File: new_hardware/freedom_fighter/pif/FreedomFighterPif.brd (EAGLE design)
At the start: 160 x 100 mm, 15 parts, among them U1 PIA6821, U4 HD68A09EP, U5 74LS74D, U9 DM74LS04N

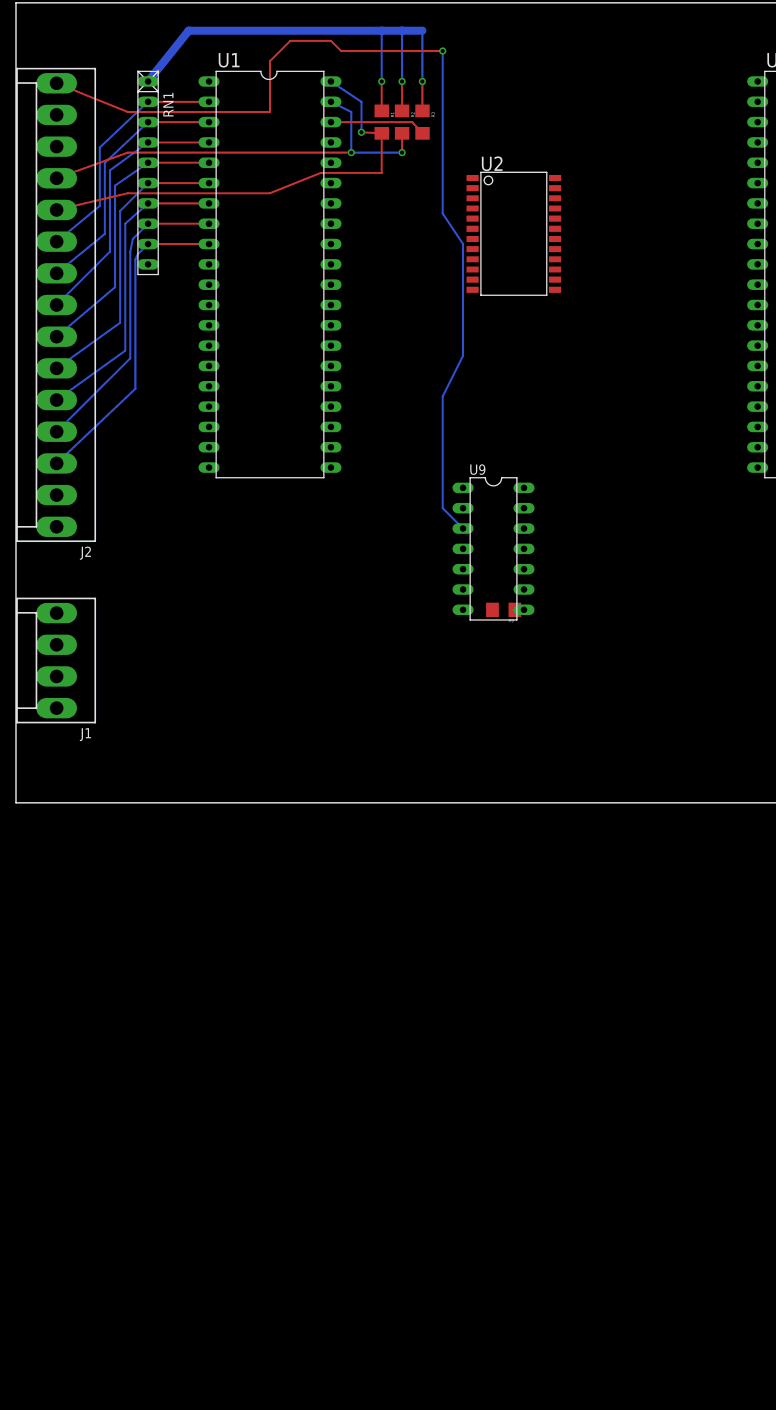
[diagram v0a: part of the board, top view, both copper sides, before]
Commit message: did more reverse engineering of freedom fighter pif board
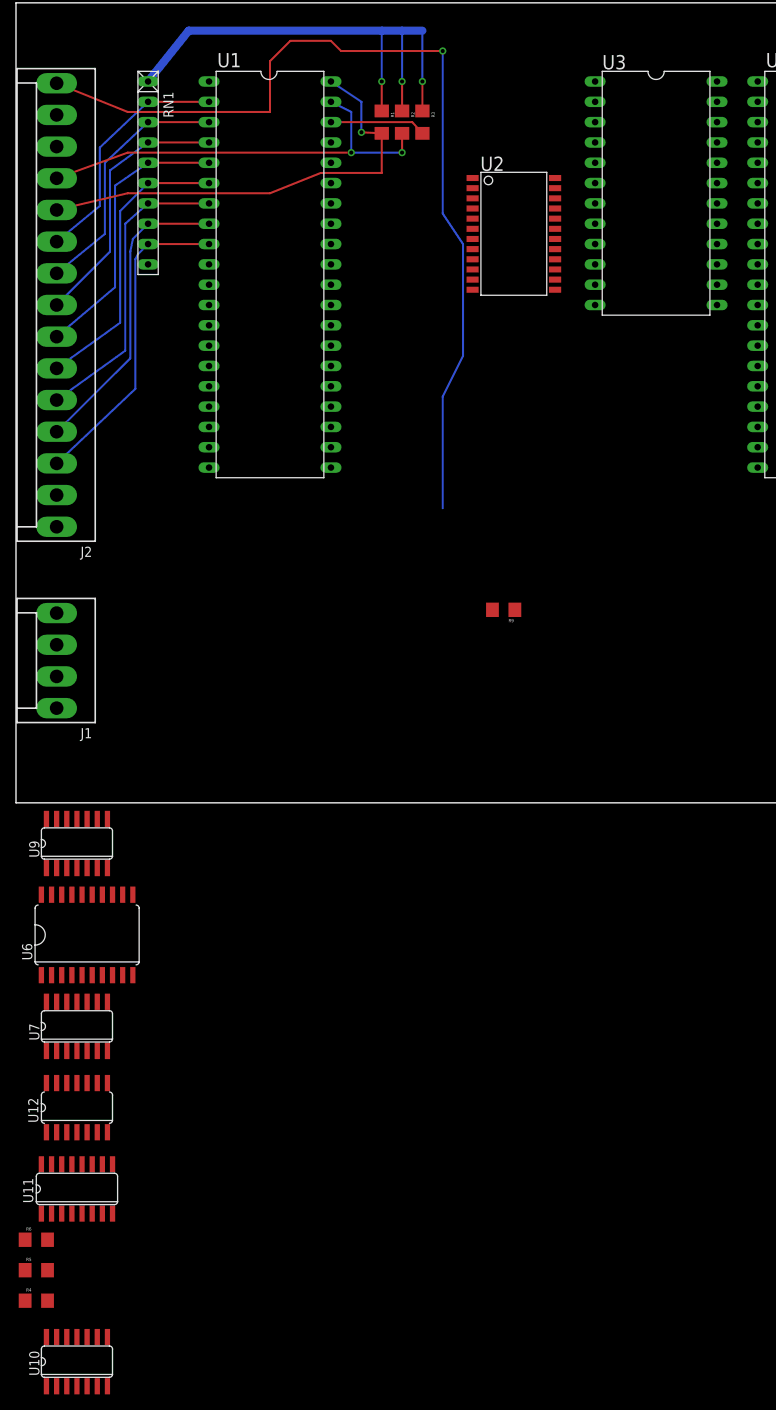
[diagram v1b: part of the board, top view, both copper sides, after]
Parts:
- added R4, R5, R6: 4.7k, SparkFun:1206
- added U10: 74LS74D, 74xx-us:SO14
- added U11: 74LS138D, 74xx-us:SO16
- added U12: 74LS125D, 74xx-eu:SO14
- added U3: 2732, memory:DIL24
- added U6: 74LS245DW, 74xx-us:SO20W
- added U7: 74LS10D, 74xx-us:SO14
- U9: value DM74LS04N -> 74LS04D; device ic-package:DIL14 -> 74xx-us:SO14
- moved U9 63.8 mm to (7.62, -5.08), turned to 0 degrees
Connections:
- removed net !IRQA: R3.2, U1.38
- new net !E: U10.2, U10.8
- new net !HALT: R4.2, U4.40
- new net !IRQA/FIRQ: R3.2, U1.38, U4.4
- new net !IRQB/NMI: R5.2, U4.2
- new net !Q: U10.6, U7.4, U7.5
- new net 4MHZ: U10.11, U10.3
- new net A13: U11.1, U4.21
- new net A14: U11.2, U4.22
- new net A15: U11.3, U4.23
- new net E: U10.9
- new net N$4: U11.6, U7.6
- new net N$6: U7.3
- new net Q: U10.12, U10.5
- new net R/!W: U1.21, U2.21, U4.32, U6.1, U7.1, U9.1
- net !IRQ: now also R6.2
- net GND: now also U10.7, U11.4, U11.5, U11.8, U12.7, U3.12, U4.1, U6.10, U7.7, U9.7
- net VCC: now also R4.1, R5.1, R6.1, U10.14, U11.16, U12.14, U3.24, U6.20, U7.14, U9.14
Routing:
- net !IRQA/FIRQ: track 0.00 -> 12.1 mm
- net !IRQA: track 12.1 -> 0.00 mm
- net EVEN/!ODD: track 119.0 -> 115.4 mm

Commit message: more reverse engineering
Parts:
- removed U3: 2732, memory:DIL24
- added C100: Unknown value, SparkFun:1206
- added DB1: DB25, mpo:A32077-ND
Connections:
- removed net N$6: U7.3
- new net !ENABLE_DAVDAK: U11.14, U12.1, U12.13
- new net !ENABLE_PIA: U1.23, U11.11
- new net !ENABLE_RAM: U11.15, U2.18
- new net !ENABLE_ROM: U11.7, U12.4
- new net !ENABLE_ROM_CE: U12.6
- new net !ENABLE_U12C: U11.9, U12.10
- new net !ENABLE_VP931_DATA: U11.12, U6.19, U9.9
- new net !VP931_RDEN: DB1.P10, U7.12
- new net !VP931_WREN: DB1.P22, U7.8
- new net D1: U4.30, U6.17
- new net D2: U4.29, U6.16
- new net D3: U4.28, U6.15
- new net D4: U4.27, U6.14
- new net D5: U4.26, U6.13
- new net D6: U12.11, U4.25, U6.12
- new net D7: U12.3, U4.24, U6.11
- new net ENABLE_VP931_DATA: U7.10, U7.13, U9.8
- new net VP931_D0: DB1.P14, U6.2
- new net VP931_D1: DB1.P15, U6.3
- new net VP931_D2: DB1.P16, U6.4
- new net VP931_D3: DB1.P17, U6.5
- new net VP931_D4: DB1.P18, U6.6
- new net VP931_D5: DB1.P19, U6.7
- new net VP931_D6: DB1.P20, U6.8
- new net VP931_D7: DB1.P21, U6.9
- new net VP931_DAK: DB1.P23, U12.2
- new net VP931_DAV: DB1.P11, U12.12
- new net W/!R: U2.20, U7.9, U9.2
- net !E: now also U7.3
- net D0: now also U6.18
- net E: now also C100.2, U4.34, U7.2
- net GND: now also DB1.P9, U12.5, U12.9, U5.10; no longer U3.12
- net Q: now also U4.35, U7.11
- net VCC: now also C100.1; no longer U3.24

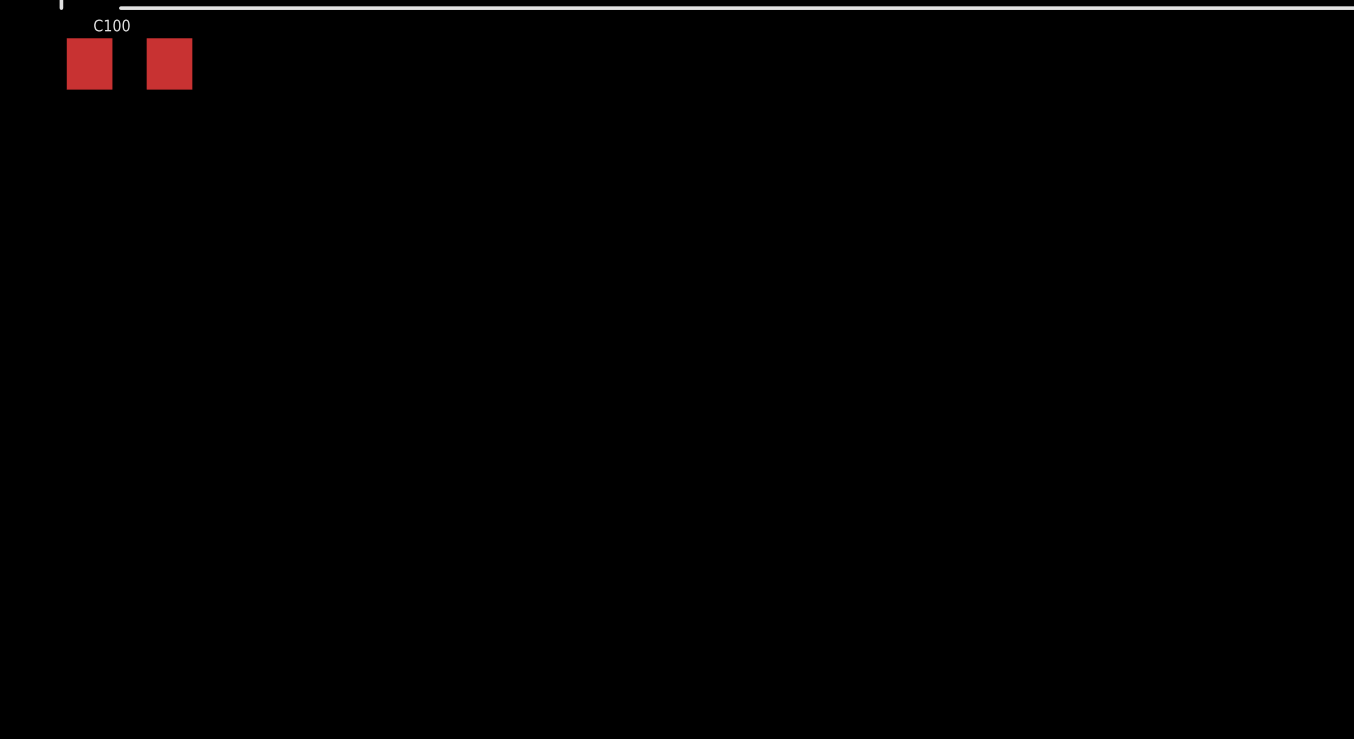
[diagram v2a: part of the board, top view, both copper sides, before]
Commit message: added FFR PIF disassembly and updated PIF schematics
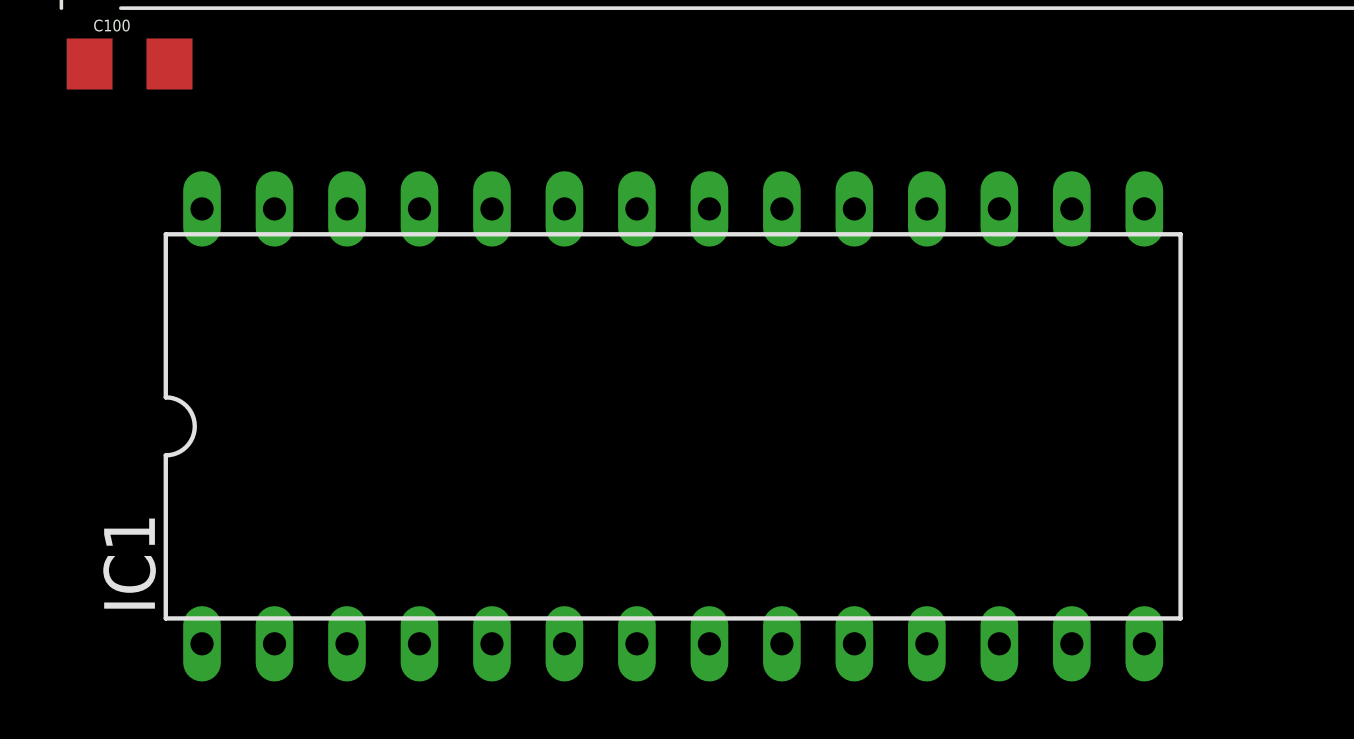
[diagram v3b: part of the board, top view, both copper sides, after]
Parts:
- added IC1: (no value), memory:DIL28
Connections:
- new net A0: IC1.10, U4.8
- new net A1: IC1.9, U4.9
- new net A10: IC1.21, U4.18
- new net A11: IC1.23, U4.19
- new net A12: IC1.2, U4.20
- new net A2: IC1.8, U4.10
- new net A3: IC1.7, U4.11
- new net A4: IC1.6, U4.12
- new net A5: IC1.5, U4.13
- new net A6: IC1.4, U4.14
- new net A7: IC1.3, U4.15
- new net A8: IC1.25, U4.16
- new net A9: IC1.24, U4.17
- net !ENABLE_ROM_CE: now also IC1.20
- net A13: now also IC1.26
- net D0: now also IC1.19
- net D1: now also IC1.18
- net D2: now also IC1.11
- net D3: now also IC1.16
- net D4: now also IC1.15
- net D5: now also IC1.13
- net D6: now also IC1.12
- net D7: now also IC1.17
- net GND: now also IC1.14, IC1.22, U4.39
- net VCC: now also IC1.1, IC1.27, IC1.28, U4.7
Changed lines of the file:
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@@
 <element name="DB1" library="mpo" package="A32077-ND" value="DB25" x="26.67" y="-90.17"/>
 <element name="C100" library="SparkFun" package="1206" value="Unknown value" x="2.54" y="-95.25"/>
+<element name="IC1" library="memory" package="DIL28" value="" x="21.59" y="-107.95"/>
 </elements>
 <signals>
@@
 <contactref element="U12" pad="9"/>
 <contactref element="U5" pad="10"/>
+<contactref element="IC1" pad="14"/>
+<contactref element="U4" pad="39"/>
+<contactref element="IC1" pad="22"/>
 <wire x1="128.8034" y1="82.55" x2="139.7" y2="90.3" width="0" layer="19" extent="1-1"/>
 <wire x1="122.6566" y1="80.01" x2="128.8034" y2="82.55" width="0" layer="19" extent="1-1"/>
-<wire x1="92.71" y1="90.17" x2="122.6566" y2="80.01" width="0" layer="19" extent="1-1"/>
+<wire x1="107.95" y1="87.63" x2="122.6566" y2="80.01" width="0" layer="19" extent="1-1"/>
+<wire x1="92.71" y1="90.17" x2="107.95" y2="87.63" width="0" layer="19" extent="1-1"/>
 <wire x1="57.0738" y1="64.135" x2="92.71" y2="90.17" width="0" layer="19" extent="1-1"/>
 <wire x1="24.13" y1="90.17" x2="57.0738" y2="64.135" width="0" layer="19" extent="1-1"/>
@@
 <wire x1="11.43" y1="-72.9234" x2="12.065" y2="-51.3334" width="0" layer="19" extent="1-1"/>
 <wire x1="32.1903" y1="-91.5924" x2="11.43" y2="-72.9234" width="0" layer="19" extent="1-1"/>
+<wire x1="20.32" y1="-100.33" x2="32.1903" y2="-91.5924" width="0" layer="19" extent="1-1"/>
+<wire x1="38.1" y1="-115.57" x2="20.32" y2="-100.33" width="0" layer="19" extent="1-1"/>
 </signal>
 <signal name="5V">
@@
 <contactref element="U10" pad="14"/>
 <contactref element="C100" pad="1"/>
+<contactref element="IC1" pad="28"/>
+<contactref element="U4" pad="7"/>
+<contactref element="IC1" pad="1"/>
+<contactref element="IC1" pad="27"/>
 <wire x1="132.08" y1="91.57" x2="135.89" y2="91.57" width="0" layer="19" extent="1-1"/>
 <wire x1="128.8034" y1="87.63" x2="132.08" y2="91.57" width="0" layer="19" extent="1-1"/>
-<wire x1="67.3862" y1="78.105" x2="128.8034" y2="87.63" width="0" layer="19" extent="1-1"/>
+<wire x1="92.71" y1="74.93" x2="128.8034" y2="87.63" width="0" layer="19" extent="1-1"/>
+<wire x1="67.3862" y1="78.105" x2="92.71" y2="74.93" width="0" layer="19" extent="1-1"/>
 <wire x1="50.8" y1="86.49" x2="67.3862" y2="78.105" width="0" layer="19" extent="1-1"/>
 <wire x1="62.36" y1="24.13" x2="67.3862" y2="78.105" width="0" layer="19" extent="1-1"/>
@@
 <wire x1="3.81" y1="-66.7766" x2="1.14" y2="-62.23" width="0" layer="19" extent="1-1"/>
 <wire x1="1.14" y1="-95.25" x2="3.81" y2="-66.7766" width="0" layer="19" extent="1-1"/>
+<wire x1="5.08" y1="-100.33" x2="1.14" y2="-95.25" width="0" layer="19" extent="1-1"/>
+<wire x1="7.62" y1="-100.33" x2="5.08" y2="-100.33" width="0" layer="19" extent="1-1"/>
+<wire x1="5.08" y1="-115.57" x2="5.08" y2="-100.33" width="0" layer="19" extent="1-1"/>
 </signal>
 <signal name="PA2">
@@
 <contactref element="U5" pad="2"/>
 <contactref element="U6" pad="18"/>
+<contactref element="IC1" pad="19"/>
 <wire x1="107.95" y1="67.31" x2="122.6566" y2="86.36" width="0" layer="19" extent="1-1"/>
 <wire x1="5.715" y1="-11.4808" x2="107.95" y2="67.31" width="0" layer="19" extent="1-1"/>
+<wire x1="27.94" y1="-100.33" x2="5.715" y2="-11.4808" width="0" layer="19" extent="1-1"/>
 </signal>
 <signal name="!IRQ">
@@
 <contactref element="U4" pad="21"/>
 <contactref element="U11" pad="1"/>
+<contactref element="IC1" pad="26"/>
 <wire x1="3.175" y1="-51.3334" x2="107.95" y2="41.91" width="0" layer="19" extent="1-1"/>
+<wire x1="10.16" y1="-100.33" x2="3.175" y2="-51.3334" width="0" layer="19" extent="1-1"/>
 </signal>
 <signal name="A14">
@@
 <contactref element="U6" pad="11"/>
 <contactref element="U12" pad="3"/>
+<contactref element="IC1" pad="17"/>
 <wire x1="14.605" y1="-11.4808" x2="107.95" y2="49.53" width="0" layer="19" extent="1-1"/>
 <wire x1="6.35" y1="-41.1734" x2="14.605" y2="-11.4808" width="0" layer="19" extent="1-1"/>
+<wire x1="33.02" y1="-100.33" x2="6.35" y2="-41.1734" width="0" layer="19" extent="1-1"/>
 </signal>
 <signal name="D6">
@@
 <contactref element="U12" pad="11"/>
 <contactref element="U6" pad="12"/>
+<contactref element="IC1" pad="12"/>
 <wire x1="13.335" y1="-11.4808" x2="107.95" y2="52.07" width="0" layer="19" extent="1-1"/>
 <wire x1="7.62" y1="-35.0266" x2="13.335" y2="-11.4808" width="0" layer="19" extent="1-1"/>
+<wire x1="33.02" y1="-115.57" x2="7.62" y2="-35.0266" width="0" layer="19" extent="1-1"/>
 </signal>
 <signal name="D5">
 <contactref element="U4" pad="26"/>
 <contactref element="U6" pad="13"/>
+<contactref element="IC1" pad="13"/>
 <wire x1="12.065" y1="-11.4808" x2="107.95" y2="54.61" width="0" layer="19" extent="1-1"/>
+<wire x1="35.56" y1="-115.57" x2="12.065" y2="-11.4808" width="0" layer="19" extent="1-1"/>
 </signal>
 <signal name="D4">
 <contactref element="U4" pad="27"/>
 <contactref element="U6" pad="14"/>
+<contactref element="IC1" pad="15"/>
 <wire x1="10.795" y1="-11.4808" x2="107.95" y2="57.15" width="0" layer="19" extent="1-1"/>
+<wire x1="38.1" y1="-100.33" x2="10.795" y2="-11.4808" width="0" layer="19" extent="1-1"/>
 </signal>
 <signal name="D3">
 <contactref element="U4" pad="28"/>
 <contactref element="U6" pad="15"/>
+<contactref element="IC1" pad="16"/>
 <wire x1="9.525" y1="-11.4808" x2="107.95" y2="59.69" width="0" layer="19" extent="1-1"/>
+<wire x1="35.56" y1="-100.33" x2="9.525" y2="-11.4808" width="0" layer="19" extent="1-1"/>
 </signal>
 <signal name="D2">
 <contactref element="U4" pad="29"/>
 <contactref element="U6" pad="16"/>
+<contactref element="IC1" pad="11"/>
 <wire x1="8.255" y1="-11.4808" x2="107.95" y2="62.23" width="0" layer="19" extent="1-1"/>
+<wire x1="30.48" y1="-115.57" x2="8.255" y2="-11.4808" width="0" layer="19" extent="1-1"/>
 </signal>
 <signal name="D1">
 <contactref element="U4" pad="30"/>
 <contactref element="U6" pad="17"/>
+<contactref element="IC1" pad="18"/>
 <wire x1="6.985" y1="-11.4808" x2="107.95" y2="64.77" width="0" layer="19" extent="1-1"/>
+<wire x1="30.48" y1="-100.33" x2="6.985" y2="-11.4808" width="0" layer="19" extent="1-1"/>
 </signal>
 <signal name="!ENABLE_VP931_DATA">
@@
 <signal name="!ENABLE_ROM_CE">
 <contactref element="U12" pad="6"/>
+<contactref element="IC1" pad="20"/>
+<wire x1="10.16" y1="-41.1734" x2="25.4" y2="-100.33" width="0" layer="19" extent="1-1"/>
 </signal>
 <signal name="!ENABLE_RAM">
@@
 <wire x1="4.445" y1="-45.1866" x2="67.3862" y2="70.485" width="0" layer="19" extent="1-1"/>
 </signal>
+<signal name="A0">
+<contactref element="U4" pad="8"/>
+<contactref element="IC1" pad="10"/>
+<wire x1="27.94" y1="-115.57" x2="92.71" y2="72.39" width="0" layer="19" extent="1-1"/>
+</signal>
+<signal name="A1">
+<contactref element="U4" pad="9"/>
+<contactref element="IC1" pad="9"/>
+<wire x1="25.4" y1="-115.57" x2="92.71" y2="69.85" width="0" layer="19" extent="1-1"/>
+</signal>
+<signal name="A2">
+<contactref element="U4" pad="10"/>
+<contactref element="IC1" pad="8"/>
+<wire x1="22.86" y1="-115.57" x2="92.71" y2="67.31" width="0" layer="19" extent="1-1"/>
+</signal>
+<signal name="A3">
+<contactref element="U4" pad="11"/>
+<contactref element="IC1" pad="7"/>
+<wire x1="20.32" y1="-115.57" x2="92.71" y2="64.77" width="0" layer="19" extent="1-1"/>
+</signal>
+<signal name="A4">
+<contactref element="U4" pad="12"/>
+<contactref element="IC1" pad="6"/>
+<wire x1="17.78" y1="-115.57" x2="92.71" y2="62.23" width="0" layer="19" extent="1-1"/>
+</signal>
+<signal name="A5">
+<contactref element="U4" pad="13"/>
+<contactref element="IC1" pad="5"/>
+<wire x1="15.24" y1="-115.57" x2="92.71" y2="59.69" width="0" layer="19" extent="1-1"/>
+</signal>
+<signal name="A6">
+<contactref element="U4" pad="14"/>
+<contactref element="IC1" pad="4"/>
+<wire x1="12.7" y1="-115.57" x2="92.71" y2="57.15" width="0" layer="19" extent="1-1"/>
+</signal>
+<signal name="A7">
+<contactref element="U4" pad="15"/>
+<contactref element="IC1" pad="3"/>
+<wire x1="10.16" y1="-115.57" x2="92.71" y2="54.61" width="0" layer="19" extent="1-1"/>
+</signal>
+<signal name="A8">
+<contactref element="U4" pad="16"/>
+<contactref element="IC1" pad="25"/>
+<wire x1="12.7" y1="-100.33" x2="92.71" y2="52.07" width="0" layer="19" extent="1-1"/>
+</signal>
+<signal name="A9">
+<contactref element="U4" pad="17"/>
+<contactref element="IC1" pad="24"/>
+<wire x1="15.24" y1="-100.33" x2="92.71" y2="49.53" width="0" layer="19" extent="1-1"/>
+</signal>
+<signal name="A10">
+<contactref element="U4" pad="18"/>
+<contactref element="IC1" pad="21"/>
+<wire x1="22.86" y1="-100.33" x2="92.71" y2="46.99" width="0" layer="19" extent="1-1"/>
+</signal>
+<signal name="A11">
+<contactref element="U4" pad="19"/>
+<contactref element="IC1" pad="23"/>
+<wire x1="17.78" y1="-100.33" x2="92.71" y2="44.45" width="0" layer="19" extent="1-1"/>
+</signal>
+<signal name="A12">
+<contactref element="U4" pad="20"/>
+<contactref element="IC1" pad="2"/>
+<wire x1="7.62" y1="-115.57" x2="92.71" y2="41.91" width="0" layer="19" extent="1-1"/>
+</signal>
 </signals>

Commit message: almost done with schematic, did some more disassembling
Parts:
- added C14, C9: 0.001uF, SparkFun:1206
- added C15: 100uF/25V, SparkFun:CPOL-RADIAL-10UF-25V
- added L1: 2.2uH, rcl:TJ8-U2
- added R10, R11, R12: 4.7k, SparkFun:1206
- added X1: CRYSTAL OSC, crystal:TC46
- DB1: value DB25 -> DB25 (FEMALE)
- U2: value (none) -> HM6116P-A
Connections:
- net !ENABLE_U12C renamed !ENABLE_ROM_C_TO_D
- removed net !ENABLE_ROM_CE: IC1.20, U12.6
- removed net 5V: J1.1
- new net !ENABLE_ROM_E_TO_F: U11.7, U12.4
- new net CS0/CS1: R10.2, U1.22, U1.24
- new net N$5: R11.2, U10.1, U10.10, U10.13, U10.4
- new net N$8: C9.2, J1.1, L1.1
- net !ENABLE_ROM: now also IC1.20, R12.2, U12.6, U12.8; no longer U11.7, U12.4
- net !IRQB/NMI: now also U1.37
- net 4MHZ: now also X1.8
- net A0: now also U1.36, U2.8
- net A1: now also U1.35, U2.7
- net A10: now also U2.19
- net A2: now also U2.6
- net A3: now also U2.5
- net A4: now also U2.4
- net A5: now also U2.3
- net A6: now also U2.2
- net A7: now also U2.1
- net A8: now also U2.23
- net A9: now also U2.22
- net D0: now also U1.33, U2.9
- net D1: now also U1.32, U2.10
- net D2: now also U1.31, U2.11
- net D3: now also U1.30, U2.13
- net D4: now also U1.29, U2.14
- net D5: now also U1.28, U2.15
- net D6: now also U1.27, U2.16
- net D7: now also U1.26, U2.17
- net E: now also U1.25
- net GND: now also C14.1, C15.2, C9.1, X1.7
- net VCC: now also C14.2, C15.1, L1.2, R10.1, R11.1, R12.1, U1.20, X1.14
